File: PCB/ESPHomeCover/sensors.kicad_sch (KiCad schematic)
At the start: 0 parts

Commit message: Add Board
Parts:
- added C20, C21, C22: 100nF 6.3V, Capacitor_SMD:C_0805_2012Metric, symbol Device:C
- added J10: WINDOW, Connector_JST:JST_XH_B3B-XH-A_1x03_P2.50mm_Vertical, symbol Connector_Generic:Conn_01x03
- added J8: Sensor UP, Connector_JST:JST_XH_B3B-XH-A_1x03_P2.50mm_Vertical, symbol Connector_Generic:Conn_01x03
- added J9: Sensor DOWN, Connector_JST:JST_XH_B3B-XH-A_1x03_P2.50mm_Vertical, symbol Connector_Generic:Conn_01x03
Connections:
- new net +3V3: C20.1, C21.1, C22.1, J10.1 (Pin_1), J8.1 (Pin_1), J9.1 (Pin_1)
- new net GND: C20.2, C21.2, C22.2, J10.2 (Pin_2), J8.2 (Pin_2), J9.2 (Pin_2)
- new net sen_down: J9.3 (Pin_3)
- new net sen_up: J8.3 (Pin_3)
- new net sen_win: J10.3 (Pin_3)
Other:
- note added: "Hall Effect/Magnetic Sensors Mfr: A1120EUA-T Mouser: 250-A1120EUA-T LCSC: C1559735"

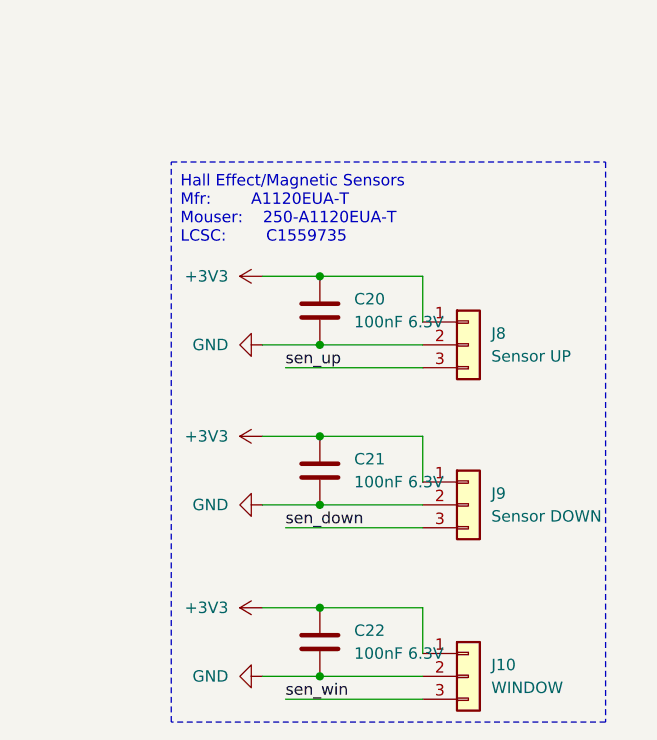
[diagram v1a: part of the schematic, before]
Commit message: small changes
change all Caps to 0603,
add bom
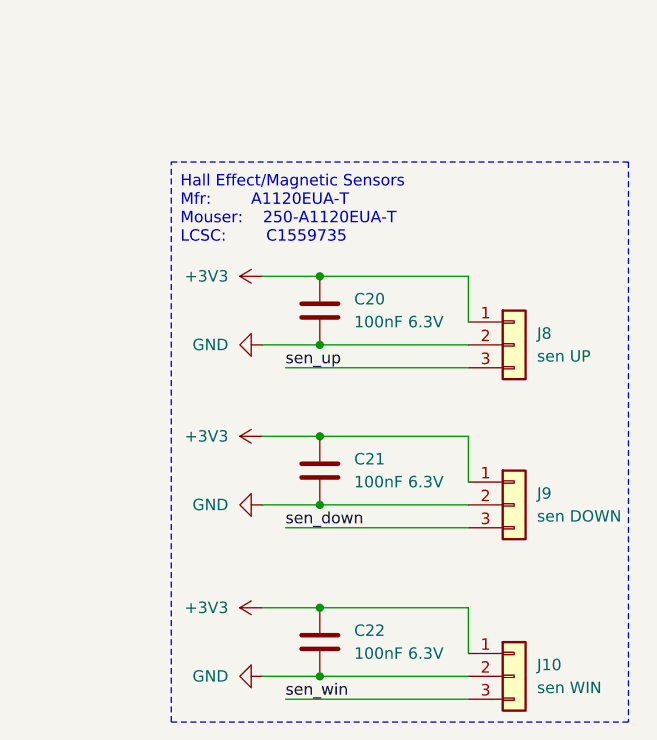
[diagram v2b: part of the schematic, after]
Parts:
- C20, C21, C22: footprint Capacitor_SMD:C_0805_2012Metric -> Capacitor_SMD:C_0603_1608Metric; LCSC C1854118 -> (none)
- J10: value WINDOW -> sen WIN
- J8: value Sensor UP -> sen UP
- J9: value Sensor DOWN -> sen DOWN
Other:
- moved on the sheet: J10, J8, J9
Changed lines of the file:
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@@
 	(title_block
 		(title "ESPHome Cover PCB")
-		(date "2024-05-08")
-		(rev "1")
+		(date "2024-05-12")
+		(rev "2")
 	)
 	(junction
@@
 	(wire
 		(pts
-			(xy 139.7 114.3) (xy 151.13 114.3)
-		)
-		(stroke
-			(width 0)
-			(type default)
-		)
-	)
-	(wire
-		(pts
-			(xy 135.89 97.79) (xy 151.13 97.79)
+			(xy 139.7 114.3) (xy 156.21 114.3)
+		)
+		(stroke
+			(width 0)
+			(type default)
+		)
+	)
+	(wire
+		(pts
+			(xy 135.89 97.79) (xy 156.21 97.79)
 		)
 		(stroke
@@
 	(wire
 		(pts
-			(xy 151.13 106.68) (xy 139.7 106.68)
-		)
-		(stroke
-			(width 0)
-			(type default)
-		)
-	)
-	(wire
-		(pts
-			(xy 151.13 74.93) (xy 151.13 69.85)
-		)
-		(stroke
-			(width 0)
-			(type default)
-		)
-	)
-	(wire
-		(pts
-			(xy 135.89 116.84) (xy 151.13 116.84)
+			(xy 156.21 106.68) (xy 139.7 106.68)
+		)
+		(stroke
+			(width 0)
+			(type default)
+		)
+	)
+	(wire
+		(pts
+			(xy 156.21 74.93) (xy 156.21 69.85)
+		)
+		(stroke
+			(width 0)
+			(type default)
+		)
+	)
+	(wire
+		(pts
+			(xy 135.89 116.84) (xy 156.21 116.84)
 		)
 		(stroke
@@
 	(wire
 		(pts
-			(xy 151.13 92.71) (xy 151.13 87.63)
-		)
-		(stroke
-			(width 0)
-			(type default)
-		)
-	)
-	(wire
-		(pts
-			(xy 151.13 69.85) (xy 139.7 69.85)
+			(xy 156.21 92.71) (xy 156.21 87.63)
+		)
+		(stroke
+			(width 0)
+			(type default)
+		)
+	)
+	(wire
+		(pts
+			(xy 156.21 69.85) (xy 139.7 69.85)
 		)
 		(stroke
@@
 	(wire
 		(pts
-			(xy 135.89 80.01) (xy 151.13 80.01)
+			(xy 135.89 80.01) (xy 156.21 80.01)
 		)
 		(stroke
@@
 	(wire
 		(pts
-			(xy 139.7 95.25) (xy 151.13 95.25)
+			(xy 139.7 95.25) (xy 156.21 95.25)
 		)
 		(stroke
@@
 	(wire
 		(pts
-			(xy 151.13 111.76) (xy 151.13 106.68)
+			(xy 156.21 111.76) (xy 156.21 106.68)
 		)
 		(stroke
@@
 	(wire
 		(pts
-			(xy 151.13 87.63) (xy 139.7 87.63)
+			(xy 156.21 87.63) (xy 139.7 87.63)
 		)
 		(stroke
@@
 	(wire
 		(pts
-			(xy 139.7 77.47) (xy 151.13 77.47)
+			(xy 139.7 77.47) (xy 156.21 77.47)
 		)
 		(stroke
@@
 	(rectangle
 		(start 123.19 57.15)
-		(end 171.45 119.38)
+		(end 173.99 119.38)
 		(stroke
 			(width 0)
@@
 			)
 		)
-		(property "Footprint" "Capacitor_SMD:C_0805_2012Metric"
+		(property "Footprint" "Capacitor_SMD:C_0603_1608Metric"
 			(at 140.6652 77.47 0)
 			(effects
@@
 			)
 		)
-		(property "LCSC" "C1854118"
+		(property "LCSC" ""
+			(at 139.7 73.66 0)
+			(effects
+				(font
+					(size 1.27 1.27)
+				)
+				(hide yes)
+			)
+		)
+		(property "Mouser" ""
 			(at 139.7 73.66 0)
 			(effects
@@
 	(symbol
 		(lib_id "Connector_Generic:Conn_01x03")
-		(at 156.21 95.25 0)
+		(at 161.29 95.25 0)
 		(unit 1)
 		(exclude_from_sim no)
@@
 		(fields_autoplaced yes)
 		(property "Reference" "J9"
-			(at 158.75 93.9799 0)
-			(effects
-				(font
-					(size 1.27 1.27)
-				)
-				(justify left)
-			)
-		)
-		(property "Value" "Sensor DOWN"
-			(at 158.75 96.5199 0)
+			(at 163.83 93.9799 0)
+			(effects
+				(font
+					(size 1.27 1.27)
+				)
+				(justify left)
+			)
+		)
+		(property "Value" "sen DOWN"
+			(at 163.83 96.5199 0)
 			(effects
 				(font
@@
 		)
 		(property "Footprint" "Connector_JST:JST_XH_B3B-XH-A_1x03_P2.50mm_Vertical"
-			(at 156.21 95.25 0)
+			(at 161.29 95.25 0)
 			(effects
 				(font
@@
 		)
 		(property "Datasheet" "~"
-			(at 156.21 95.25 0)
+			(at 161.29 95.25 0)
 			(effects
 				(font
@@
 		)
 		(property "Description" "Generic connector, single row, 01x03, script generated (kicad-library-utils/schlib/autogen/connector/)"
-			(at 156.21 95.25 0)
+			(at 161.29 95.25 0)
+			(effects
+				(font
+					(size 1.27 1.27)
+				)
+				(hide yes)
+			)
+		)
+		(property "Mouser" ""
+			(at 161.29 95.25 0)
 			(effects
 				(font
@@
 			)
 		)
-		(property "Footprint" "Capacitor_SMD:C_0805_2012Metric"
+		(property "Footprint" "Capacitor_SMD:C_0603_1608Metric"
 			(at 140.6652 95.25 0)
 			(effects
@@
 			)
 		)
-		(property "LCSC" "C1854118"
+		(property "LCSC" ""
+			(at 139.7 91.44 0)
+			(effects
+				(font
+					(size 1.27 1.27)
+				)
+				(hide yes)
+			)
+		)
+		(property "Mouser" ""
 			(at 139.7 91.44 0)
 			(effects
@@
 			)
 		)
-		(property "Footprint" "Capacitor_SMD:C_0805_2012Metric"
+		(property "Footprint" "Capacitor_SMD:C_0603_1608Metric"
 			(at 140.6652 114.3 0)
 			(effects
@@
 			)
 		)
-		(property "LCSC" "C1854118"
+		(property "LCSC" ""
+			(at 139.7 110.49 0)
+			(effects
+				(font
+					(size 1.27 1.27)
+				)
+				(hide yes)
+			)
+		)
+		(property "Mouser" ""
 			(at 139.7 110.49 0)
 			(effects
@@
 	(symbol
 		(lib_id "Connector_Generic:Conn_01x03")
-		(at 156.21 114.3 0)
+		(at 161.29 114.3 0)
 		(unit 1)
 		(exclude_from_sim no)
@@
 		(fields_autoplaced yes)
 		(property "Reference" "J10"
-			(at 158.75 113.0299 0)
-			(effects
-				(font
-					(size 1.27 1.27)
-				)
-				(justify left)
-			)
-		)
-		(property "Value" "WINDOW"
-			(at 158.75 115.5699 0)
+			(at 163.83 113.0299 0)
+			(effects
+				(font
+					(size 1.27 1.27)
+				)
+				(justify left)
+			)
+		)
+		(property "Value" "sen WIN"
+			(at 163.83 115.5699 0)
 			(effects
 				(font
@@
 		)
 		(property "Footprint" "Connector_JST:JST_XH_B3B-XH-A_1x03_P2.50mm_Vertical"
-			(at 156.21 114.3 0)
+			(at 161.29 114.3 0)
 			(effects
 				(font
@@
 		)
 		(property "Datasheet" "~"
-			(at 156.21 114.3 0)
+			(at 161.29 114.3 0)
 			(effects
 				(font
@@
 		)
 		(property "Description" "Generic connector, single row, 01x03, script generated (kicad-library-utils/schlib/autogen/connector/)"
-			(at 156.21 114.3 0)
+			(at 161.29 114.3 0)
+			(effects
+				(font
+					(size 1.27 1.27)
+				)
+				(hide yes)
+			)
+		)
+		(property "Mouser" ""
+			(at 161.29 114.3 0)
 			(effects
 				(font
@@
 	(symbol
 		(lib_id "Connector_Generic:Conn_01x03")
-		(at 156.21 77.47 0)
+		(at 161.29 77.47 0)
 		(unit 1)
 		(exclude_from_sim no)
@@
 		(fields_autoplaced yes)
 		(property "Reference" "J8"
-			(at 158.75 76.1999 0)
-			(effects
-				(font
-					(size 1.27 1.27)
-				)
-				(justify left)
-			)
-		)
-		(property "Value" "Sensor UP"
-			(at 158.75 78.7399 0)
+			(at 163.83 76.1999 0)
+			(effects
+				(font
+					(size 1.27 1.27)
+				)
+				(justify left)
+			)
+		)
+		(property "Value" "sen UP"
+			(at 163.83 78.7399 0)
 			(effects
 				(font
@@
 		)
 		(property "Footprint" "Connector_JST:JST_XH_B3B-XH-A_1x03_P2.50mm_Vertical"
-			(at 156.21 77.47 0)
+			(at 161.29 77.47 0)
 			(effects
 				(font
@@
 		)
 		(property "Datasheet" "~"
-			(at 156.21 77.47 0)
+			(at 161.29 77.47 0)
 			(effects
 				(font
@@
 		)
 		(property "Description" "Generic connector, single row, 01x03, script generated (kicad-library-utils/schlib/autogen/connector/)"
-			(at 156.21 77.47 0)
-			(effects
-				(font
+			(at 161.29 77.47 0)
+			(effects
+				(font
+					(size 1.27 1.27)
+				)
+				(hide yes)
+			)
+		)
+		(property "Mouser" ""
+			(at 161.29 77.47 0)
+			(effects
+				(font

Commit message: update PCB
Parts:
- C20, C21, C22: Mouser Part Number (none) -> 581-06036C104JAT2A
- J10: value sen WIN -> WIN
- J8: value sen UP -> UP
- J9: value sen DOWN -> DOWN
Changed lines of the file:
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@@
 		(title "ESPHome Cover PCB")
 		(date "2024-05-12")
-		(rev "2")
+		(rev "1")
 	)
 	(junction
@@
 			)
 		)
+		(property "Mouser Part Number" "581-06036C104JAT2A"
+			(at 139.7 73.66 0)
+			(effects
+				(font
+					(size 1.27 1.27)
+				)
+				(hide yes)
+			)
+		)
 		(pin "1"
 		)
@@
 			)
 		)
-		(property "Value" "sen DOWN"
+		(property "Value" "DOWN"
 			(at 163.83 96.5199 0)
 			(effects
@@
 			)
 		)
+		(property "Mouser Part Number" "581-06036C104JAT2A"
+			(at 139.7 91.44 0)
+			(effects
+				(font
+					(size 1.27 1.27)
+				)
+				(hide yes)
+			)
+		)
 		(pin "1"
 		)
@@
 			)
 		)
+		(property "Mouser Part Number" "581-06036C104JAT2A"
+			(at 139.7 110.49 0)
+			(effects
+				(font
+					(size 1.27 1.27)
+				)
+				(hide yes)
+			)
+		)
 		(pin "1"
 		)
@@
 			)
 		)
-		(property "Value" "sen WIN"
+		(property "Value" "WIN"
 			(at 163.83 115.5699 0)
 			(effects
@@
 			)
 		)
-		(property "Value" "sen UP"
+		(property "Value" "UP"
 			(at 163.83 78.7399 0)
 			(effects

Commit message: update PCB
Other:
- company: (none) -> Tim
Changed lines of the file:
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@@
 		(date "2024-05-12")
 		(rev "1")
+		(company "Tim")
 	)
 	(junction
